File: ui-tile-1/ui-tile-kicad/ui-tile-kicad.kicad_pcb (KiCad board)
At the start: 4 copper layers, 59 parts, among them Q1 2N7002, SW1 SKRPABE010, SW2 SKRPABE010, SW3 EC11E15244G1, SW4 EC11E15244G1, SW5 EC11E15244G1, SW6 EC11E15244G1, U1 RP2040, U2 W25Q16JVUXIQ, U3 NCP1117ST33T3G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

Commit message: finished first pass of pcb layout
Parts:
- moved R9 31.2 mm to (153.8, 127.2), turned to 0 degrees
- moved R8 29.4 mm to (153.9, 131.8), turned to 0 degrees
- moved LED2 27.3 mm to (156.9, 127.2), turned to 180 degrees
- moved LED1 25.5 mm to (156.8, 131.8), turned to 180 degrees
- moved D2 16.4 mm to (144.4, 129.8)
- moved SW1 12.6 mm to (158.6, 138.2)
- moved R6 11.5 mm to (161.0, 136.8), turned to 90 degrees
- moved SW2 10.3 mm to (152.4, 138.2)
- moved R7 9.54 mm to (154.6, 136.8), turned to 90 degrees
- moved H2 1.50 mm to (131.6, 63.5)
- moved C10 1.35 mm to (113.0, 133.8)
- moved R10 0.91 mm to (146.8, 66.8)
- moved H1 0.87 mm to (131.6, 129.5)
- moved R12 0.82 mm to (146.4, 65.2)
- moved C15 0.63 mm to (115.2, 133.8)
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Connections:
- U1 pad 2: /headers/MISO -> /headers/CS
- U1 pad 3: /headers/CS -> /headers/SCK
- U1 pad 4: /headers/SCK -> /headers/MISO
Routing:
- net /headers/CS: track 0.00 -> 101.1 mm, vias 0 -> 2
- net /headers/SCK: track 0.00 -> 97.9 mm, vias 0 -> 2
- net Net-(LED4-DOUT): track 0.00 -> 95.6 mm, vias 0 -> 2
- net /headers/MISO: track 0.00 -> 90.6 mm, vias 0 -> 2
- net /headers/IRQ: track 0.00 -> 90.3 mm, vias 0 -> 4
- net /headers/MOSI: track 0.00 -> 90.0 mm, vias 0 -> 4
- net /lcd/BL: track 0.00 -> 84.8 mm, vias 0 -> 4
- net +5V: track 0.00 -> 80.1 mm, vias 0 -> 2
- net /leds/LED_3V3: track 0.00 -> 66.8 mm, vias 0 -> 4
- net /rp2040/RUN: track 0.00 -> 63.5 mm, vias 0 -> 4
- net /lcd/CS: track 14.2 -> 74.5 mm, vias 0 -> 2
- net /lcd/MOSI: track 18.8 -> 75.9 mm, vias 0 -> 2
- net /lcd/DC: track 16.1 -> 72.7 mm, vias 0 -> 2
- net /lcd/RES: track 13.4 -> 70.0 mm, vias 0 -> 2
- net /lcd/SCK: track 22.6 -> 78.2 mm, vias 0 -> 2
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- added copper zone on In2.Cu, net +3V3
- added copper zone on B.Cu, net VSYS
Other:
- board outline added: 72.4 x 81.3 mm
- board text added: "+3.3V"
- board text added: "BOOT"
- board text added: "RESET"
- board text added: "VSYS +5V"

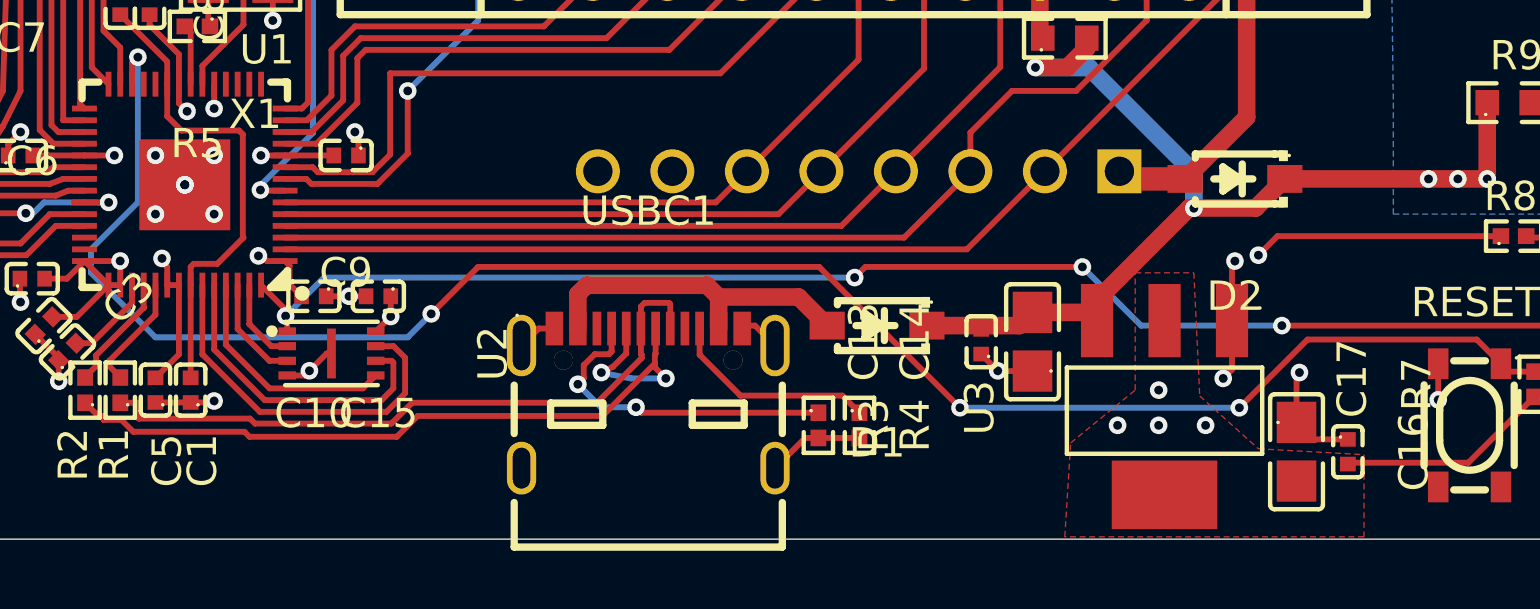
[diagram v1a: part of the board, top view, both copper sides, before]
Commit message: moved regulator away from board edge
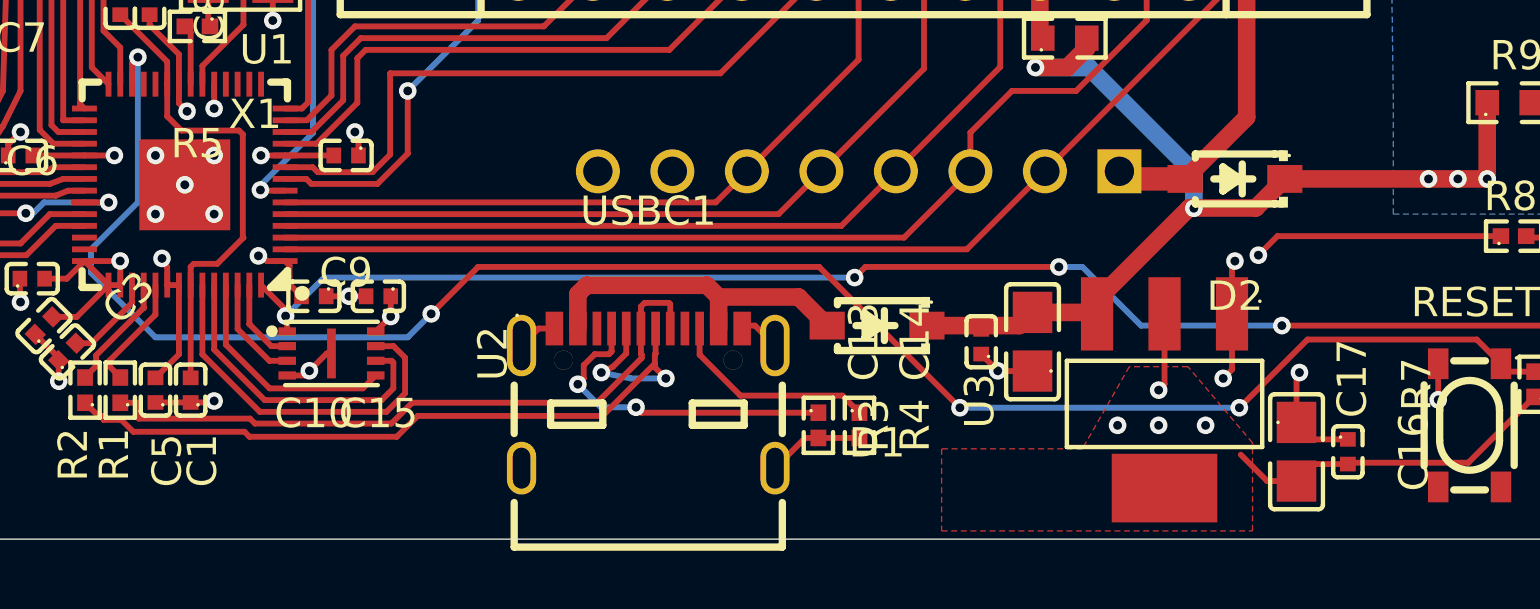
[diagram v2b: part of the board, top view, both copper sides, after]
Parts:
- moved U3 0.23 mm to (142.0, 137.4)
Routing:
- net +3V3: track 47.6 -> 54.3 mm
- net GND: vias 35 -> 34
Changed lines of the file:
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@@
 		(capping no)
 		(filling no)
-		(zone_defaults)
 		(pcbplotparams
 			(layerselection 0x00000000_00000000_55555555_5755f5ff)
@@
 	(footprint "jlcpcb:SOT-223-3_L6.5-W3.4-P2.30-LS7.0-BR"
 		(layer "F.Cu")
-		(at 142 137.6 90)
+		(at 142 137.37 90)
 		(property "Reference" "U3"
 			(at 0 -6.3 90)
@@
 	)
 	(segment
-		(start 131.6 138.63)
-		(end 129.75 138.63)
-		(width 0.2)
-		(layer "F.Cu")
-		(net "GND")
-	)
-	(segment
 		(start 102.98 133.2)
 		(end 102.98 133.98)
@@
 	)
 	(segment
+		(start 129.75 138.63)
+		(end 131.6 138.63)
+		(width 0.2)
+		(layer "F.Cu")
+		(net "GND")
+	)
+	(segment
 		(start 114.78 133.8)
 		(end 114 133.8)
@@
 	)
 	(via
-		(at 108.6 130)
-		(size 0.6)
-		(drill 0.3)
-		(layers "F.Cu" "B.Cu")
-		(net "GND")
-	)
-	(via
 		(at 103 128.2)
 		(size 0.6)
@@
 	)
 	(segment
+		(start 146.5 140.1)
+		(end 145.5 140.1)
+		(width 0.2)
+		(layer "F.Cu")
+		(net "+3V3")
+	)
+	(segment
 		(start 106 133.42)
 		(end 105.18 132.6)
@@
 	)
 	(segment
+		(start 148.25 139.52)
+		(end 147.08 139.52)
+		(width 0.2)
+		(layer "F.Cu")
+		(net "+3V3")
+	)
+	(segment
 		(start 105.18 132.6)
 		(end 106.394407 132.6)
@@
 	)
 	(segment
+		(start 142 136.8)
+		(end 141.8 137)
+		(width 0.2)
+		(layer "F.Cu")
+		(net "+3V3")
+	)
+	(segment
 		(start 108 133.42)
 		(end 108 132.8)
@@
 	)
 	(segment
+		(start 142 134.63)
+		(end 142 136.8)
+		(width 0.2)
+		(layer "F.Cu")
+		(net "+3V3")
+	)
+	(segment
 		(start 111.177289 132.422711)
 		(end 111.11029 132.422711)
@@
 	)
 	(segment
+		(start 147.08 139.52)
+		(end 146.5 140.1)
+		(width 0.2)
+		(layer "F.Cu")
+		(net "+3V3")
+	)
+	(segment
 		(start 145.85 131.75)
 		(end 145.2 132.4)
@@
 	)
 	(segment
+		(start 145.5 140.1)
+		(end 144.6 139.2)
+		(width 0.2)
+		(layer "F.Cu")
+		(net "+3V3")
+	)
+	(segment
 		(start 112.17 133.39)
 		(end 112.17 132.75)
@@
 	)
 	(segment
-		(start 136.4 67.058)
-		(end 132.842 63.5)
-		(width 0.2)
-		(layer "F.Cu")
-		(net "/headers/MISO")
-	)
-	(segment
-		(start 112.02 131.4)
-		(end 130.982 131.4)
-		(width 0.2)
-		(layer "F.Cu")
-		(net "/headers/MISO")
-	)
-	(segment
-		(start 136.4 125.982)
-		(end 136.4 109.2)
-		(width 0.2)
-		(layer "F.Cu")
-		(net "/headers/MISO")
-	)
-	(segment
-		(start 132.842 129.54)
-		(end 136.4 125.982)
-		(width 0.2)
-		(layer "F.Cu")
-		(net "/headers/MISO")
-	)
-	(segment
-		(start 130.982 131.4)
-		(end 132.842 129.54)
-		(width 0.2)
-		(layer "F.Cu")
-		(net "/headers/MISO")
-	)
-	(segment
-		(start 136.4 104.6)
-		(end 136.4 67.058)
-		(width 0.2)
-		(layer "F.Cu")
-		(net "/headers/MISO")
-	)
-	(via
-		(at 136.4 104.6)
-		(size 0.6)
-		(drill 0.3)
-		(layers "F.Cu" "B.Cu")
-		(net "/headers/MISO")
-	)
-	(via
-		(at 136.4 109.2)
-		(size 0.6)
-		(drill 0.3)
-		(layers "F.Cu" "B.Cu")
-		(net "/headers/MISO")
-	)
-	(segment
-		(start 136.4 109.2)
-		(end 136.4 104.6)
-		(width 0.2)
-		(layer "B.Cu")
-		(net "/headers/MISO")
-	)
-	(segment
 		(start 141.39 69.925635)
 		(end 141.39 66.968)
@@
 	)
 	(segment
+		(start 136.4 67.058)
+		(end 132.842 63.5)
+		(width 0.2)
+		(layer "F.Cu")
+		(net "/headers/MISO")
+	)
+	(segment
+		(start 112.02 131.4)
+		(end 130.982 131.4)
+		(width 0.2)
+		(layer "F.Cu")
+		(net "/headers/MISO")
+	)
+	(segment
+		(start 136.4 125.982)
+		(end 136.4 109.2)
+		(width 0.2)
+		(layer "F.Cu")
+		(net "/headers/MISO")
+	)
+	(segment
+		(start 132.842 129.54)
+		(end 136.4 125.982)
+		(width 0.2)
+		(layer "F.Cu")
+		(net "/headers/MISO")
+	)
+	(segment
+		(start 130.982 131.4)
+		(end 132.842 129.54)
+		(width 0.2)
+		(layer "F.Cu")
+		(net "/headers/MISO")
+	)
+	(segment
+		(start 136.4 104.6)
+		(end 136.4 67.058)
+		(width 0.2)
+		(layer "F.Cu")
+		(net "/headers/MISO")
+	)
+	(via
+		(at 136.4 104.6)
+		(size 0.6)
+		(drill 0.3)
+		(layers "F.Cu" "B.Cu")
+		(net "/headers/MISO")
+	)
+	(via
+		(at 136.4 109.2)
+		(size 0.6)
+		(drill 0.3)
+		(layers "F.Cu" "B.Cu")
+		(net "/headers/MISO")
+	)
+	(segment
+		(start 136.4 109.2)
+		(end 136.4 104.6)
+		(width 0.2)
+		(layer "B.Cu")
+		(net "/headers/MISO")
+	)
+	(segment
 		(start 131.57 71.77)
 		(end 131.57 64.768)
@@
 	)
 	(segment
-		(start 139.2 132.8)
-		(end 131.8 132.8)
+		(start 159.67 136.1)
+		(end 158.37 134.8)
 		(width 0.2)
 		(layer "F.Cu")
@@
 	)
 	(segment
-		(start 159.67 136.1)
-		(end 158.37 134.8)
+		(start 112.09 134.31)
+		(end 111.2 133.42)
 		(width 0.2)
 		(layer "F.Cu")
@@
 	)
 	(segment
-		(start 112.09 134.31)
-		(end 111.2 133.42)
+		(start 112.09 135)
+		(end 112.09 134.31)
 		(width 0.2)
 		(layer "F.Cu")
@@
 	)
 	(segment
-		(start 112.09 135)
-		(end 112.09 134.31)
+		(start 138.4 132.8)
+		(end 131.8 132.8)
 		(width 0.2)
 		(layer "F.Cu")
@@
 	)
 	(via
-		(at 139.2 132.8)
+		(at 138.4 132.8)
 		(size 0.6)
 		(drill 0.3)
@@
 	)
 	(segment
-		(start 146 134.8)
-		(end 141.2 134.8)
+		(start 138.4 132.8)
+		(end 139.2 132.8)
 		(width 0.2)
 		(layer "B.Cu")
@@
 	)
 	(segment
-		(start 113.347047 133.163235)
-		(end 112.035913 134.474369)
+		(start 141.2 134.8)
+		(end 146 134.8)
 		(width 0.2)
 		(layer "B.Cu")
@@
 	)
 	(segment
-		(start 141.2 134.8)
-		(end 139.2 132.8)
+		(start 139.2 132.8)
+		(end 141.2 134.8)
+		(width 0.2)
+		(layer "B.Cu")
+		(net "/rp2040/QSPI_SS")
+	)
+	(segment
+		(start 113.347047 133.163235)
+		(end 112.035913 134.474369)
 		(width 0.2)
 		(layer "B.Cu")
@@
 		(net "+3V3")
 		(layer "F.Cu")
-		(name "GND Plane")
+		(name "+3V3 Top")
 		(hatch edge 0.5)
 		(priority 1)
@@
 		(polygon
 			(pts
-				(xy 148.8 139.2) (xy 148.8 142) (xy 138.6 142) (xy 138.8 138.8) (xy 141 137) (xy 141 133) (xy 143 133)
-				(xy 143.2 137.2) (xy 145.2 139)
+				(xy 145 141.8) (xy 145 138.8) (xy 142.8 136.2) (xy 140.8 136.2) (xy 139.2 139) (xy 134.4 139) (xy 134.4 141.8)
 			)
 		)

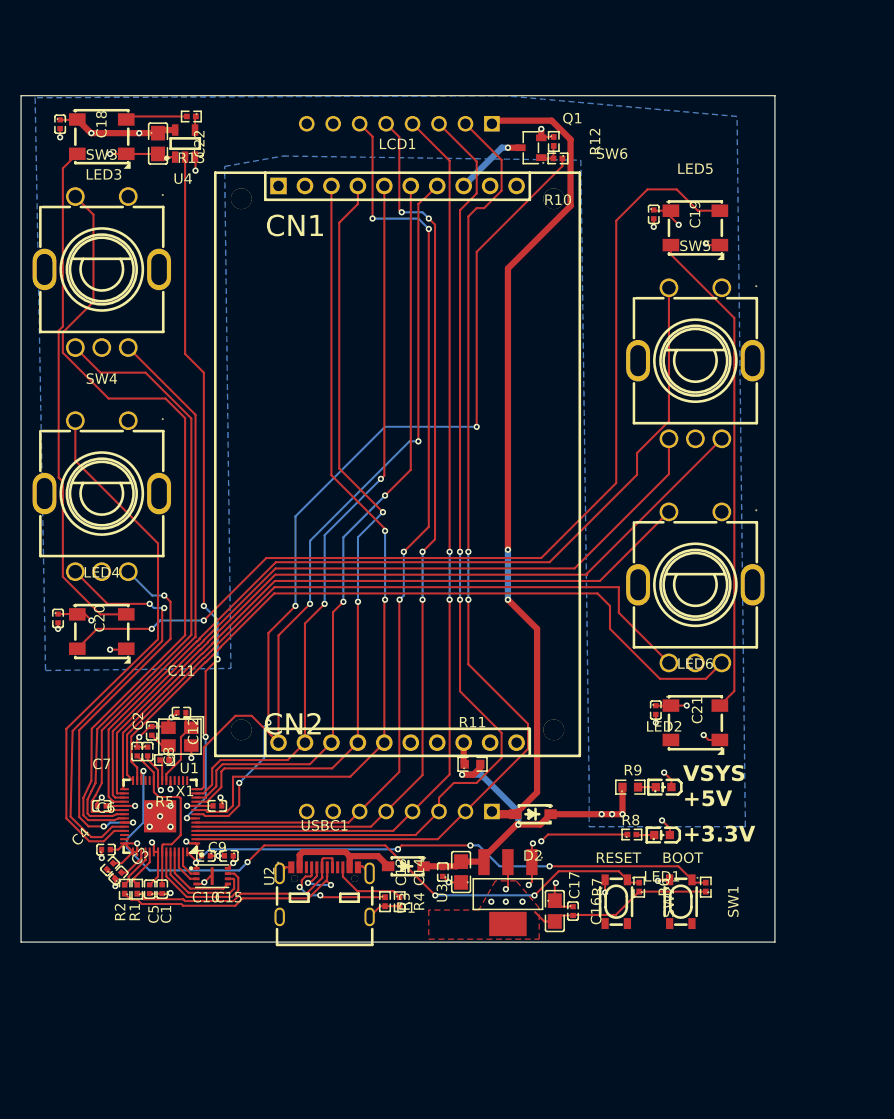
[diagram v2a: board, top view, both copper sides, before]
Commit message: Added mounting holes
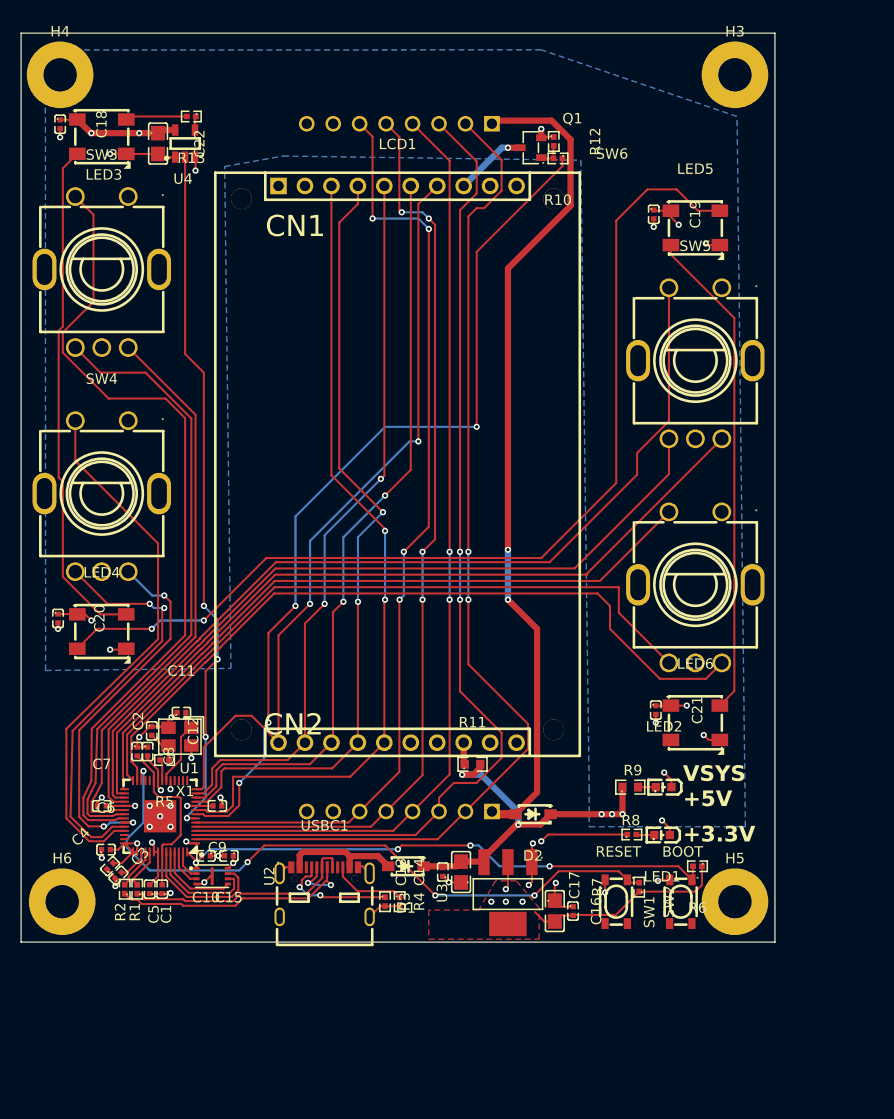
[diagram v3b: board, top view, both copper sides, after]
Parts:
- added H3: MountingHole_Pad, MountingHole:MountingHole_3.2mm_M3_Pad, F.Cu at (163.8, 58.8)
- added H4: MountingHole_Pad, MountingHole:MountingHole_3.2mm_M3_Pad, F.Cu at (99.0, 58.8)
- added H5: MountingHole_Pad, MountingHole:MountingHole_3.2mm_M3_Pad, F.Cu at (163.8, 138.2)
- added H6: MountingHole_Pad, MountingHole:MountingHole_3.2mm_M3_Pad, F.Cu at (99.2, 138.2)
- moved R6 2.15 mm to (160.2, 134.8), turned to 180 degrees
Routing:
- net +3V3: track 54.3 -> 56.0 mm
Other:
- board size 72.4 x 81.3 mm -> 72.4 x 87.3 mm

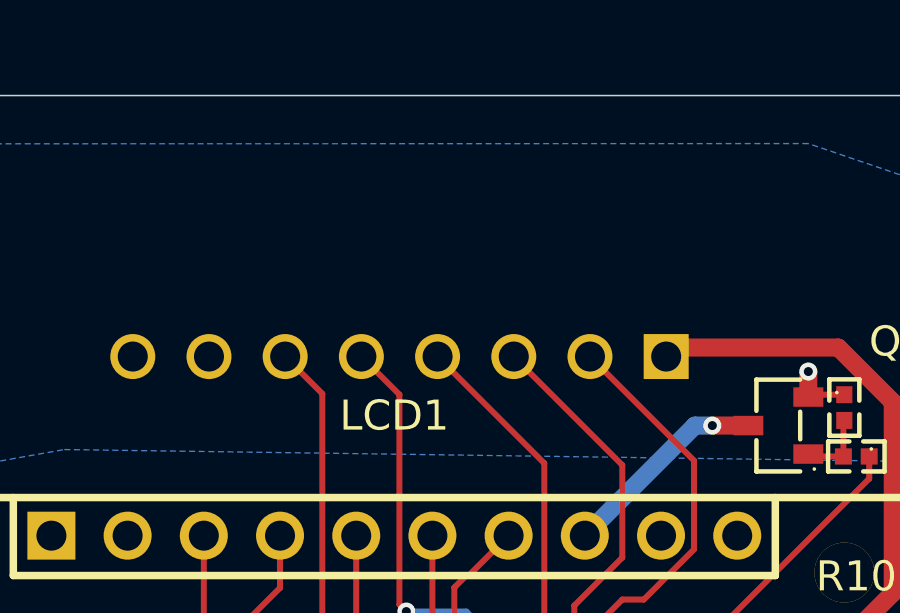
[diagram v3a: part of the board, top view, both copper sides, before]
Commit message: added fpc connector
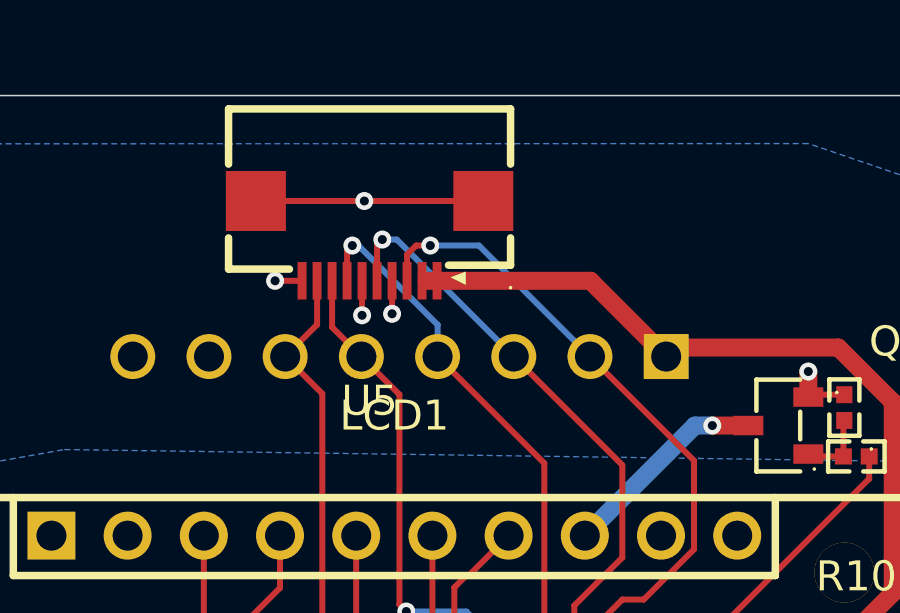
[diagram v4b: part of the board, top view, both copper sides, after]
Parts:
- added U5: 05A20L10P, jlcpcb:FPC-SMD_10P-P0.50_05A20L10P, F.Cu at (130.6, 59.6)
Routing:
- net GND: track 59.3 -> 70.4 mm, vias 34 -> 38
- net +5V: track 80.1 -> 89.1 mm
- net /headers/CS: track 101.1 -> 109.7 mm, vias 2 -> 3
- net /headers/SCK: track 97.9 -> 105.4 mm, vias 2 -> 3
- net /headers/MISO: track 90.6 -> 96.8 mm, vias 2 -> 3
- net /headers/IRQ: track 90.3 -> 93.3 mm
- net /headers/MOSI: track 90.0 -> 92.9 mm
